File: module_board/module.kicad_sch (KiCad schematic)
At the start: 0 parts

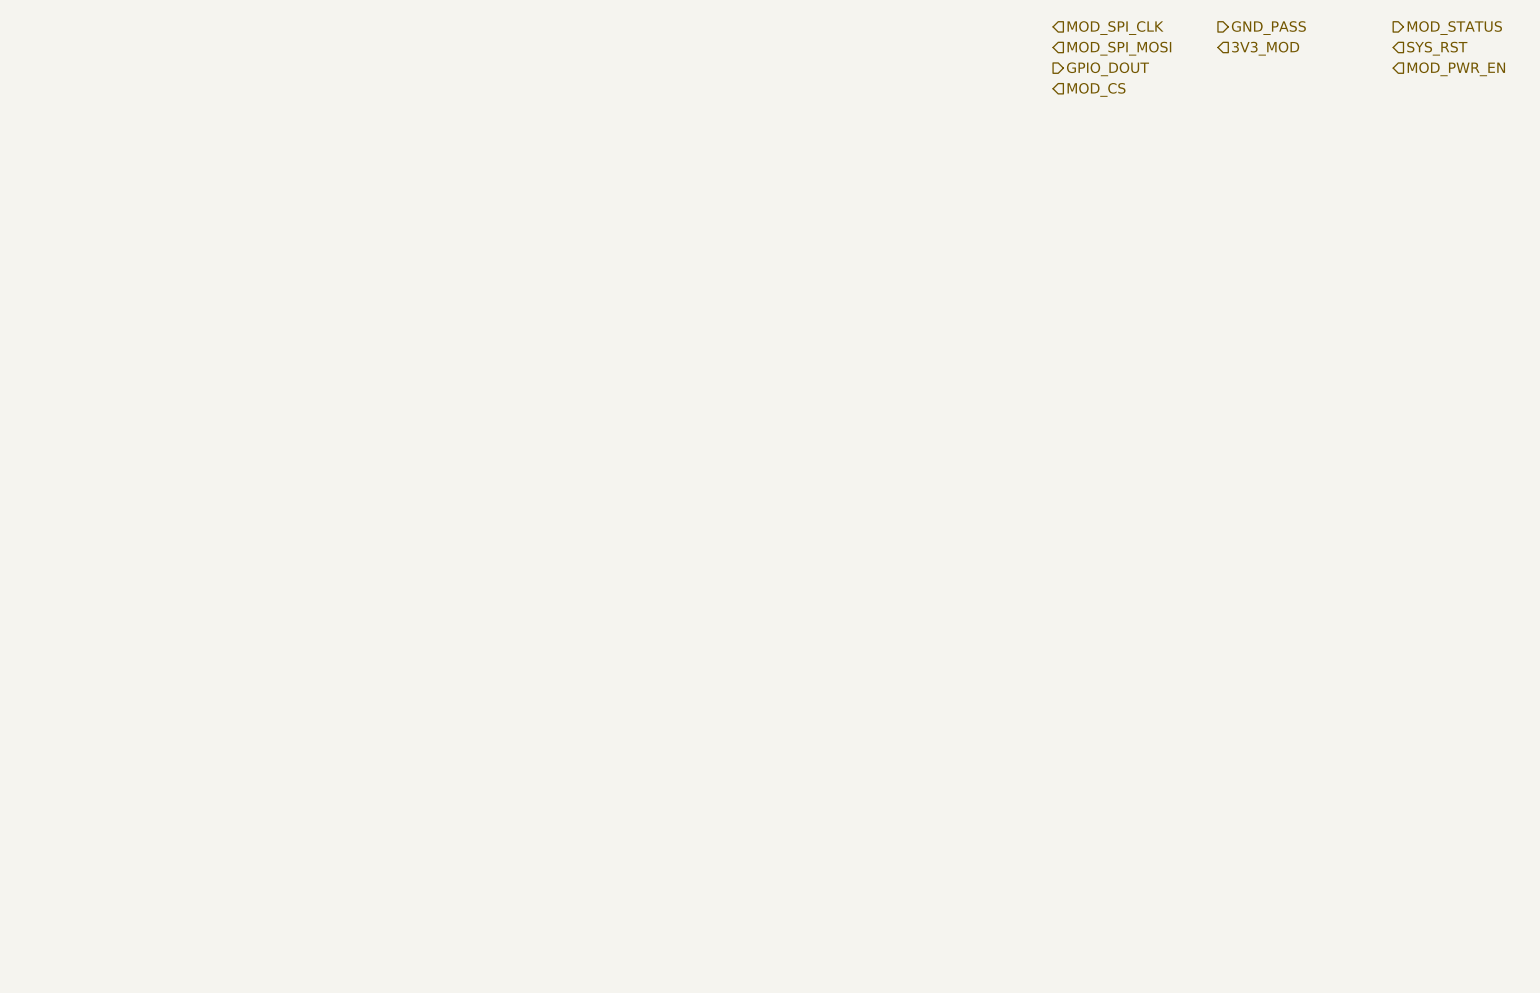
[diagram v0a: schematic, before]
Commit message: feat: finish all essential schematics (i think?)
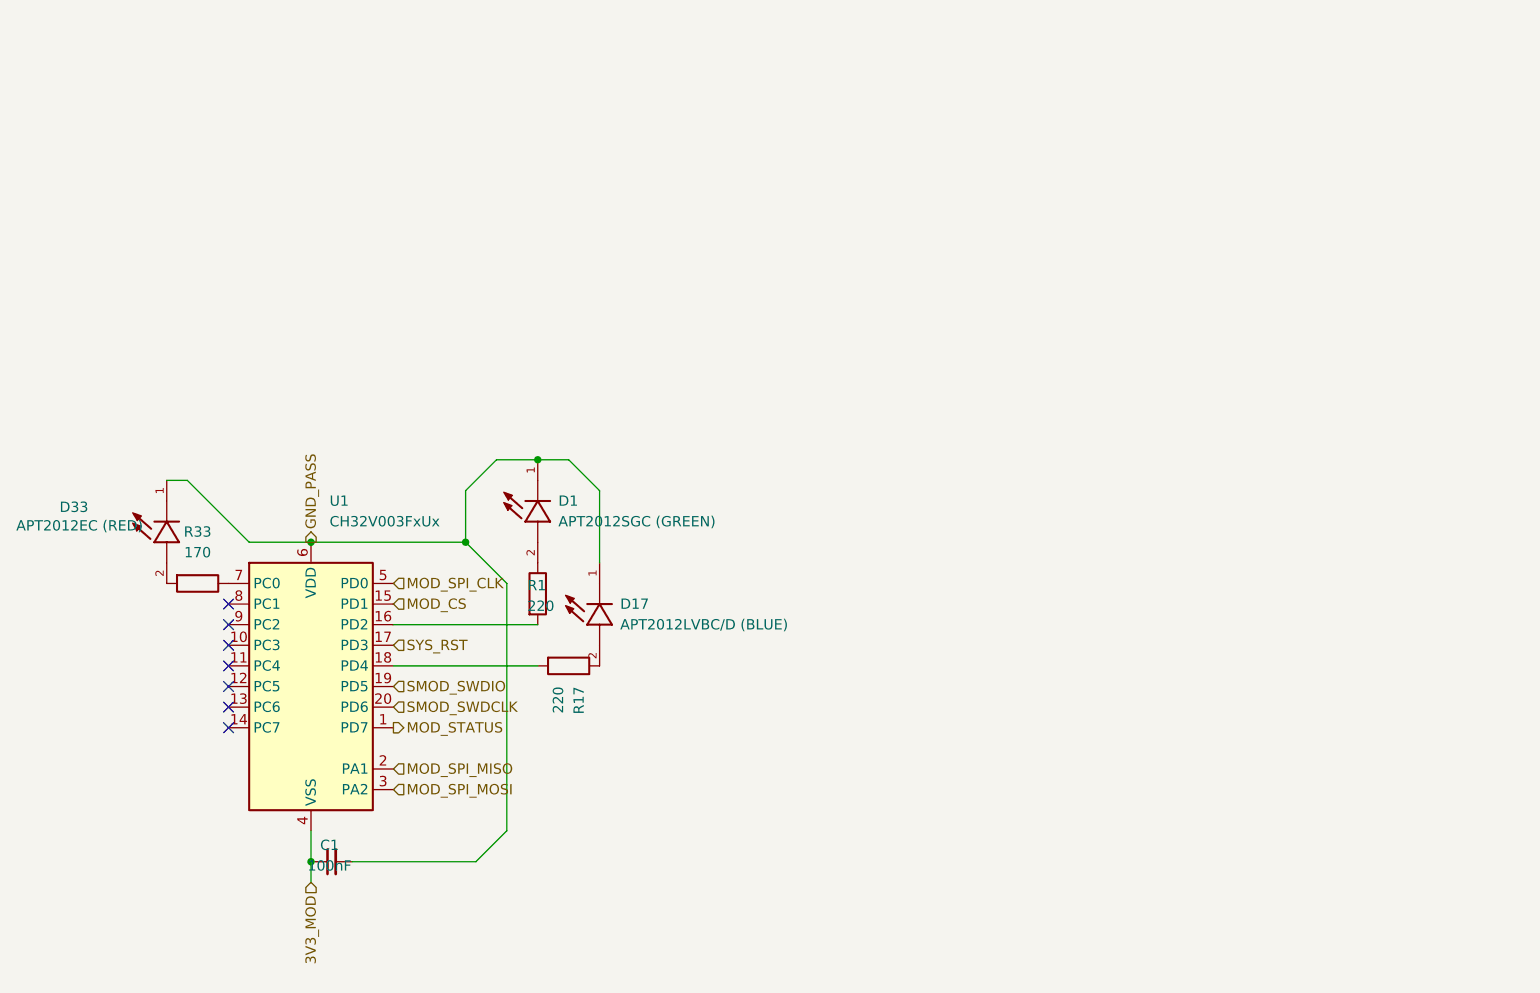
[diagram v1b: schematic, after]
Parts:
- added C1: 100nF, Capacitor_SMD:C_0402_1005Metric, symbol Device:C_Small
- added D1: APT2012SGC (GREEN), APT2012SGC:APT2012SGC, symbol APT2012SGC:APT2012SGC
- added D17: APT2012LVBC/D (BLUE), APT2012SGC:APT2012SGC, symbol APT2012SGC:APT2012SGC
- added D33: APT2012EC (RED), APT2012SGC:APT2012SGC, symbol APT2012SGC:APT2012SGC
- added R1, R17: 220, Resistor_SMD:R_0402_1005Metric, symbol Device:R
- added R33: 170, Resistor_SMD:R_0402_1005Metric, symbol Device:R
- added U1: CH32V003FxUx, Package_DFN_QFN:QFN-20-1EP_3x3mm_P0.4mm_EP1.65x1.65mm, symbol MCU_WCH_RiscV:CH32V003FxUx
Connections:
- net 3V3_MOD: now also C1.1, U1.21 (VSS), U1.4 (VSS)
- net GND_PASS: now also C1.2, D1.1, D17.1, D33.1, U1.6 (VDD)
- net MOD_CS: now also U1.15 (PD1)
- net MOD_SPI_CLK: now also U1.5 (PD0)
- net MOD_SPI_MOSI: now also U1.3 (PA2)
- net MOD_STATUS: now also U1.1 (PD7)
- net SYS_RST: now also U1.17 (PD3)
- new net: D17.2, R17.1
- new net: D1.2, R1.1
- new net: R1.2, U1.16 (PD2)
- new net: R17.2, U1.18 (PD4)
- new net: R33.1, U1.7 (PC0)
- new net: D33.2, R33.2
- new net MOD_SPI_MISO: U1.2 (PA1)
- new net SMOD_SWDCLK: U1.20 (PD6)
- new net SMOD_SWDIO: U1.19 (PD5)
- no-connect marks 0 -> 7

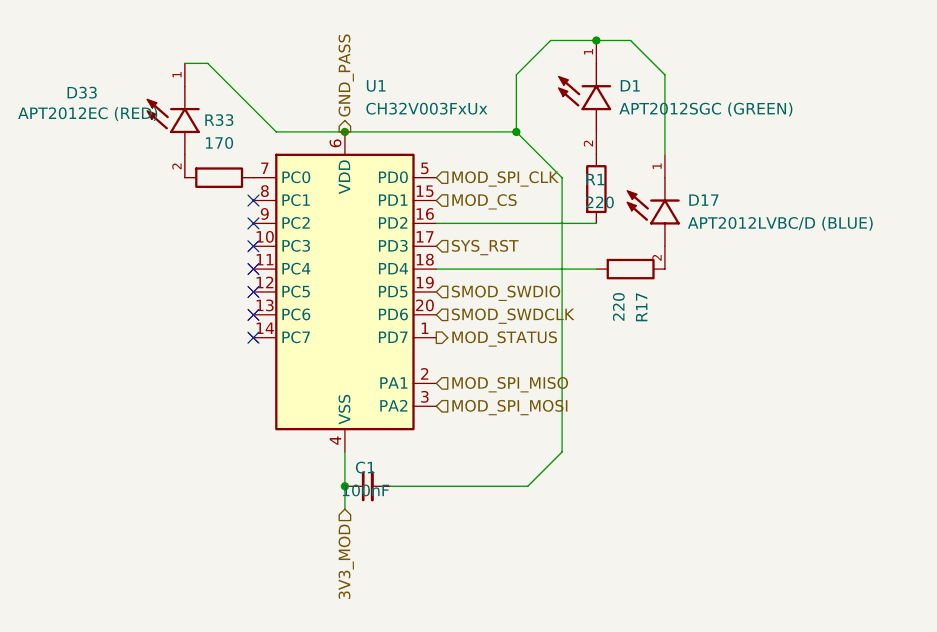
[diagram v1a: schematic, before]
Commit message: ruined all the traces on MB
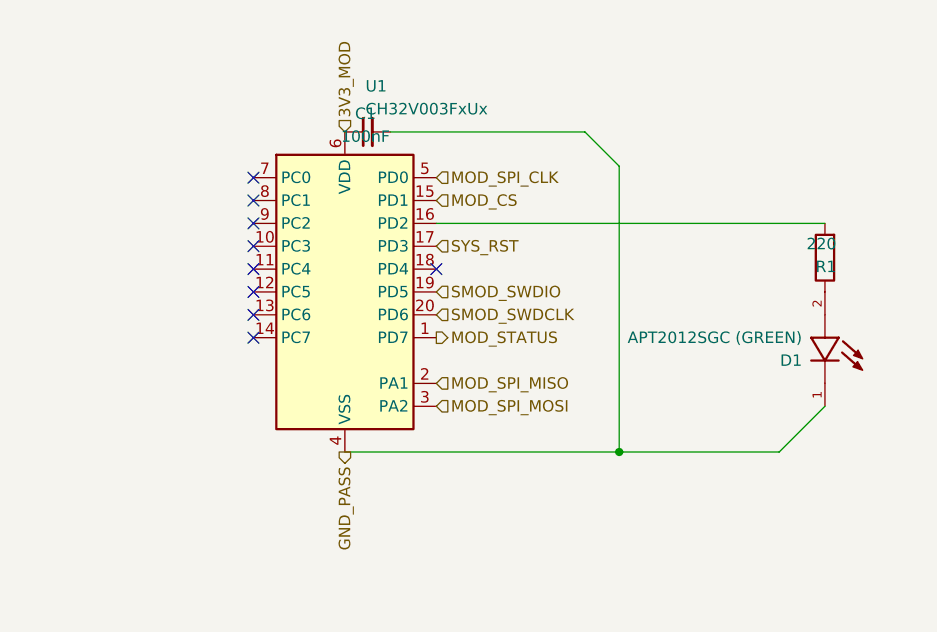
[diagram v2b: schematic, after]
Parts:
- removed D17: APT2012LVBC/D (BLUE), APT2012SGC:APT2012SGC, symbol APT2012SGC:APT2012SGC
- removed D33: APT2012EC (RED), APT2012SGC:APT2012SGC, symbol APT2012SGC:APT2012SGC
- removed R17: 220, Resistor_SMD:R_0402_1005Metric, symbol Device:R
- removed R33: 170, Resistor_SMD:R_0402_1005Metric, symbol Device:R
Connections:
- net 3V3_MOD: now also U1.6 (VDD); no longer U1.21 (VSS), U1.4 (VSS)
- net GND_PASS: now also U1.21 (VSS), U1.4 (VSS); no longer U1.6 (VDD)
- no-connect marks 7 -> 9
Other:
- moved on the sheet: C1, D1, R1
